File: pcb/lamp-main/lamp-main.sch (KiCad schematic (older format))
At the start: 29 parts, among them IC1 ATMEGA328P, IC2 DNP(LM1117_3.3), P1 VLED_IN, P10 V_IN, P2 AVR_ISP, P3 SERIAL, P4 LEDSTACK, P5 LEDSTACK, P6 LEDSTACK, P7 USER-INPUT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

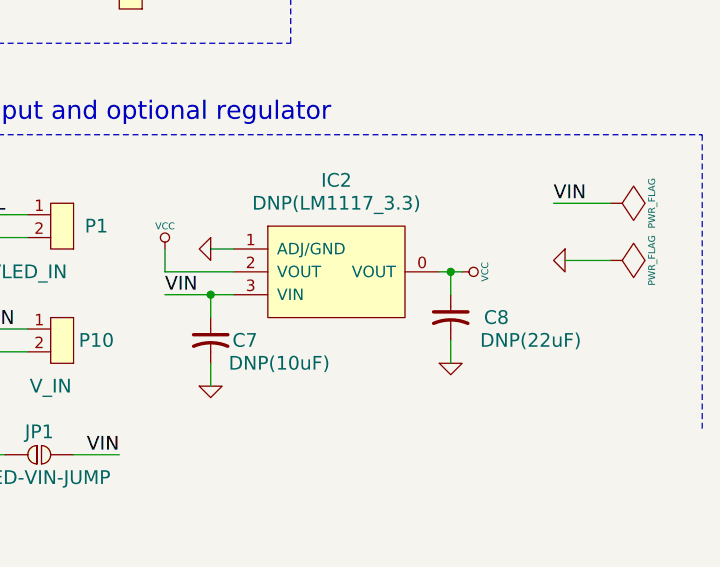
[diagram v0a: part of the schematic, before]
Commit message: add changes found after first iMac powerup since 2014
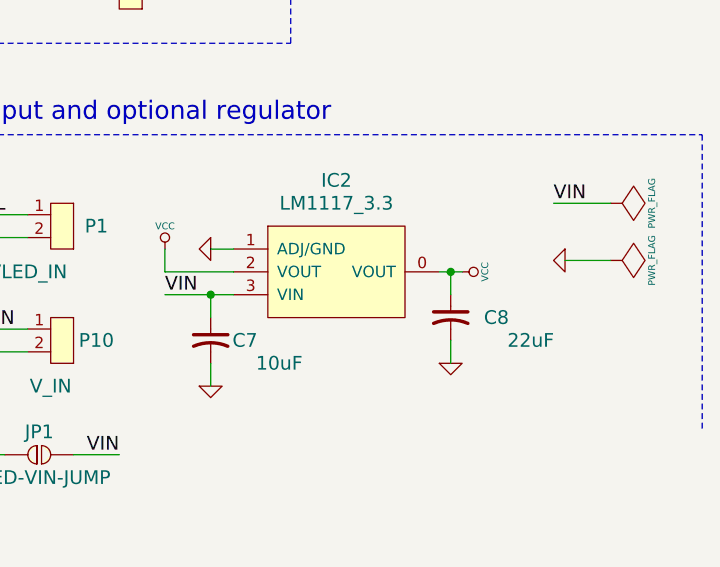
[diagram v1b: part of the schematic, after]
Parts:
- C1, C2, C3, C4, C5, C6, C9: footprint (none) -> capacitor:0603(1608m)-CHIP-CAP
- C7: value DNP(10uF) -> 10uF; footprint (none) -> capacitor:1206(3216m)-CHIP-CAP
- C8: value DNP(22uF) -> 22uF; footprint (none) -> capacitor:1206(3216m)-CHIP-CAP
- IC1: footprint (none) -> qfp:TQFP32_P0.8mm; Distrib. Link (none) -> http://www.digikey.com/product-detail/en/ATMEGA328P-AU/ATME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; Distrib. Part (none) -> ATMEGA328P-AU-ND; Distributor Link http://www.digikey.com/product-detail/en/ATMEGA328P-AU/ATME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 -> (none); Distributor Part ATMEGA328P-AU-ND -> (none); Manuf. Part (none) -> ATMEGA328P-AU; Manufacturer Part ATMEGA328P-AU -> (none)
- IC2: value DNP(LM1117_3.3) -> LM1117_3.3; footprint (none) -> sot:SOT223
- JP1: footprint (none) -> jumper:SOLDER-JUMPER_1-WAY
- LED1, LED2: footprint (none) -> led:0603(1608m)-SM-LED
- P1, P10, P8: footprint (none) -> sip:SIP2
- P2: footprint (none) -> connect-thru:2x3-ARRAY_P100mil
- P3: footprint (none) -> sip:SIP6
- P4, P5, P6, P7: footprint (none) -> sip:SIP5
- R1, R2, R3, R6, R7: footprint (none) -> resistor:0603(1608m)-CHIP-RESISTOR
- Y1: footprint (none) -> crystal:ABRACON-ABM2_xtal
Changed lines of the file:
@@
 F 0 "IC1" H 2650 3400 60  0000 C CNN
 F 1 "ATMEGA328P" H 3700 1050 60  0000 C CNN
-F 2 "" H 3350 2250 60  0000 C CNN
-F 3 "" H 3350 2250 60  0000 C CNN
+F 2 "qfp:TQFP32_P0.8mm" H 3350 2250 60  0001 C CNN
+F 3 "" H 3350 2250 60  0001 C CNN
 F 4 "Atmel" H 3350 2250 60  0001 C CNN "Manufacturer"
-F 5 "ATMEGA328P-AU" H 3350 2250 60  0001 C CNN "Manufacturer Part"
+F 5 "ATMEGA328P-AU" H 3350 2250 60  0001 C CNN "Manuf. Part"
 F 6 "Digikey" H 3350 2250 60  0001 C CNN "Distributor"
-F 7 "ATMEGA328P-AU-ND" H 3350 2250 60  0001 C CNN "Distributor Part"
-F 8 "http://www.digikey.com/product-detail/en/ATMEGA328P-AU/ATMEGA328P-AU-ND/1832260" H 3350 2250 60  0001 C CNN "Distributor Link"
+F 7 "ATMEGA328P-AU-ND" H 3350 2250 60  0001 C CNN "Distrib. Part"
+F 8 "http://www.digikey.com/product-detail/en/ATMEGA328P-AU/ATMEGA328P-AU-ND/1832260" H 3350 2250 60  0001 C CNN "Distrib. Link"
 	1    3350 2250
 	1    0    0    -1
@@
 F 0 "P2" H 1700 5300 60  0000 C CNN
 F 1 "AVR_ISP" H 2100 5300 60  0000 C CNN
-F 2 "" H 1950 5100 60  0001 C CNN
+F 2 "connect-thru:2x3-ARRAY_P100mil" H 1950 5100 60  0001 C CNN
 F 3 "" H 1950 5100 60  0001 C CNN
 	1    1950 5100
@@
 F 0 "P3" H 4050 5550 60  0000 C CNN
 F 1 "SERIAL" H 4000 5450 60  0000 C CNN
-F 2 "" H 4100 5050 60  0001 C CNN
+F 2 "sip:SIP6" H 4100 5050 60  0001 C CNN
 F 3 "" H 4100 5050 60  0001 C CNN
 	1    4050 5050
@@
 F 0 "Y1" V 2200 2700 60  0000 C CNN
 F 1 "8MHz" V 2100 2700 60  0000 C CNN
-F 2 "" H 2150 2500 60  0001 C CNN
+F 2 "crystal:ABRACON-ABM2_xtal" H 2150 2500 60  0001 C CNN
 F 3 "http://www.abracon.com/Resonators/abm2.pdf" H 2150 2500 60  0001 C CNN
 F 4 "Abracon Corporation" H 2150 2500 60  0001 C CNN "Manufacturer"
@@
 F 0 "C2" H 1350 2550 60  0000 C CNN
 F 1 "24pF" H 1600 2550 60  0000 C CNN
-F 2 "" H 1500 2400 60  0001 C CNN
+F 2 "capacitor:0603(1608m)-CHIP-CAP" H 1500 2400 60  0001 C CNN
 F 3 "" H 1500 2400 60  0001 C CNN
 F 4 "Samsung" H 1500 2400 60  0001 C CNN "Manufacturer"
@@
 F 0 "C6" H 1950 2450 60  0000 C CNN
 F 1 "0.1uF" H 1950 2350 60  0000 C CNN
-F 2 "" H 2100 2250 60  0001 C CNN
+F 2 "capacitor:0603(1608m)-CHIP-CAP" H 2100 2250 60  0001 C CNN
 F 3 "" H 2100 2250 60  0001 C CNN
 F 4 "On hand" H 2100 2250 60  0001 C CNN "Distributor"
@@
 F 0 "C1" V 1650 1750 60  0000 C CNN
 F 1 "0.1uF" V 1550 1750 60  0000 C CNN
-F 2 "" H 1350 1750 60  0001 C CNN
+F 2 "capacitor:0603(1608m)-CHIP-CAP" H 1350 1750 60  0001 C CNN
 F 3 "" H 1350 1750 60  0001 C CNN
 F 4 "On Hand" H 1350 1750 60  0001 C CNN "Distributor"
@@
 F 0 "C4" V 1950 1750 60  0000 C CNN
 F 1 "0.1uF" V 1850 1750 60  0000 C CNN
-F 2 "" H 1650 1750 60  0001 C CNN
+F 2 "capacitor:0603(1608m)-CHIP-CAP" H 1650 1750 60  0001 C CNN
 F 3 "" H 1650 1750 60  0001 C CNN
 F 4 "On hand" H 1650 1750 60  0001 C CNN "Distributor"
@@
 F 0 "C5" V 2250 1750 60  0000 C CNN
 F 1 "0.1uF" V 2150 1750 60  0000 C CNN
-F 2 "" H 1950 1750 60  0001 C CNN
+F 2 "capacitor:0603(1608m)-CHIP-CAP" H 1950 1750 60  0001 C CNN
 F 3 "" H 1950 1750 60  0001 C CNN
 F 4 "On hand" H 1950 1750 60  0001 C CNN "Distributor"
@@
 F 0 "P1" H 7350 3900 60  0000 C CNN
 F 1 "VLED_IN" H 7050 3700 60  0000 C CNN
-F 2 "" H 7100 3700 60  0001 C CNN
+F 2 "sip:SIP2" H 7100 3700 60  0001 C CNN
 F 3 "" H 7100 3700 60  0001 C CNN
 	1    7150 3900
@@
 P 8400 4100
 F 0 "IC2" H 8400 4500 60  0000 C CNN
-F 1 "DNP(LM1117_3.3)" H 8400 4400 60  0000 C CNN
-F 2 "" H 8400 4100 60  0001 C CNN
+F 1 "LM1117_3.3" H 8400 4400 60  0000 C CNN
+F 2 "sot:SOT223" H 8400 4100 60  0001 C CNN
 F 3 "http://www.diodes.com/datasheets/AZ1117C.pdf" H 8400 4100 60  0001 C CNN
 F 4 "Diodes Incorporated" H 8400 4100 60  0001 C CNN "Manufacturer"
@@
 P 7850 4400
 F 0 "C7" V 7850 4550 60  0000 C CNN
-F 1 "DNP(10uF)" V 7950 4700 60  0000 C CNN
-F 2 "" H 7850 4400 60  0001 C CNN
+F 1 "10uF" V 7950 4700 60  0000 C CNN
+F 2 "capacitor:1206(3216m)-CHIP-CAP" H 7850 4400 60  0001 C CNN
 F 3 "" H 7850 4400 60  0001 C CNN
 F 4 "Taiyo Yuden" H 7850 4400 60  0001 C CNN "Manufacturer"
@@
 P 8900 4300
 F 0 "C8" V 8900 4500 60  0000 C CNN
-F 1 "DNP(22uF)" V 9000 4650 60  0000 C CNN
-F 2 "" H 8900 4300 60  0001 C CNN
+F 1 "22uF" V 9000 4650 60  0000 C CNN
+F 2 "capacitor:1206(3216m)-CHIP-CAP" H 8900 4300 60  0001 C CNN
 F 3 "" H 8900 4300 60  0001 C CNN
 F 4 "Taiyo Yuden" H 8900 4300 60  0001 C CNN "Manufacturer"
@@
 F 0 "R2" H 5400 1400 60  0000 C CNN
 F 1 "10kΩ" H 5700 1400 60  0000 C CNN
-F 2 "" H 5350 1700 60  0001 C CNN
+F 2 "resistor:0603(1608m)-CHIP-RESISTOR" H 5350 1700 60  0001 C CNN
 F 3 "" H 5350 1700 60  0001 C CNN
 F 4 "On hand" H 5350 1700 60  0001 C CNN "Distributor"
@@
 F 0 "R3" H 5400 1500 60  0000 C CNN
 F 1 "10kΩ" H 5700 1500 60  0000 C CNN
-F 2 "" H 5350 1800 60  0001 C CNN
+F 2 "resistor:0603(1608m)-CHIP-RESISTOR" H 5350 1800 60  0001 C CNN
 F 3 "" H 5350 1800 60  0001 C CNN
 F 4 "On hand" H 5350 1800 60  0001 C CNN "Distributor"
@@
 F 0 "P4" H 7650 1500 60  0000 C CNN
 F 1 "LEDSTACK" H 7800 1400 60  0000 C CNN
-F 2 "" H 7500 1200 60  0001 C CNN
+F 2 "sip:SIP5" H 7500 1200 60  0001 C CNN
 F 3 "" H 7500 1200 60  0001 C CNN
 	1    7450 1300
@@
 F 0 "P5" H 7650 2200 60  0000 C CNN
 F 1 "LEDSTACK" H 7800 2100 60  0000 C CNN
-F 2 "" H 7500 1900 60  0001 C CNN
+F 2 "sip:SIP5" H 7500 1900 60  0001 C CNN
 F 3 "" H 7500 1900 60  0001 C CNN
 	1    7450 2000
@@
 F 0 "P6" H 7650 2900 60  0000 C CNN
 F 1 "LEDSTACK" H 7800 2800 60  0000 C CNN
-F 2 "" H 7500 2600 60  0001 C CNN
+F 2 "sip:SIP5" H 7500 2600 60  0001 C CNN
 F 3 "" H 7500 2600 60  0001 C CNN
 	1    7450 2700
@@
 F 0 "C3" H 1350 2450 60  0000 C CNN
 F 1 "24pF" H 1600 2450 60  0000 C CNN
-F 2 "" H 1500 2600 60  0001 C CNN
+F 2 "capacitor:0603(1608m)-CHIP-CAP" H 1500 2600 60  0001 C CNN
 F 3 "" H 1500 2600 60  0001 C CNN
 F 4 "Samsung Electro-Mechanics America, Inc" H 1500 2600 60  0001 C CNN "Manufacturer"
@@
 F 0 "R6" H 1950 3250 60  0000 C CNN
 F 1 "1kΩ" H 2150 3250 60  0000 C CNN
-F 2 "" H 2000 3350 60  0001 C CNN
+F 2 "resistor:0603(1608m)-CHIP-RESISTOR" H 2000 3350 60  0001 C CNN
 F 3 "" H 2000 3350 60  0001 C CNN
 F 4 "On hand" H 2000 3350 60  0001 C CNN "Distributor"
@@
 F 0 "LED1" H 1450 3450 60  0000 C CNN
 F 1 "RED" H 1750 3450 60  0000 C CNN
-F 2 "" H 1600 3350 60  0001 C CNN
+F 2 "led:0603(1608m)-SM-LED" H 1600 3350 60  0001 C CNN
 F 3 "" H 1600 3350 60  0001 C CNN
 F 4 "On hand" H 1600 3350 60  0001 C CNN "Distributor"
@@
 F 0 "R7" H 1950 3500 60  0000 C CNN
 F 1 "1kΩ" H 2150 3500 60  0000 C CNN
-F 2 "" H 2000 3600 60  0001 C CNN
+F 2 "resistor:0603(1608m)-CHIP-RESISTOR" H 2000 3600 60  0001 C CNN
 F 3 "" H 2000 3600 60  0001 C CNN
 F 4 "On hand" H 2000 3600 60  0001 C CNN "Distributor"
@@
 F 0 "LED2" H 1450 3700 60  0000 C CNN
 F 1 "RED" H 1750 3700 60  0000 C CNN
-F 2 "" H 1600 3600 60  0001 C CNN
+F 2 "led:0603(1608m)-SM-LED" H 1600 3600 60  0001 C CNN
 F 3 "" H 1600 3600 60  0001 C CNN
 F 4 "On hand" H 1600 3600 60  0001 C CNN "Distributor"
@@
 F 0 "R1" H 5400 1300 60  0000 C CNN
 F 1 "10kΩ" H 5700 1300 60  0000 C CNN
-F 2 "" H 5350 1600 60  0001 C CNN
+F 2 "resistor:0603(1608m)-CHIP-RESISTOR" H 5350 1600 60  0001 C CNN
 F 3 "" H 5350 1600 60  0001 C CNN
 F 4 "On hand" H 5350 1600 60  0001 C CNN "Distributor"
@@
 F 0 "C9" H 3450 5150 60  0000 C CNN
 F 1 "0.1uF" H 3700 5150 60  0000 C CNN
-F 2 "" H 3750 5300 60  0001 C CNN
+F 2 "capacitor:0603(1608m)-CHIP-CAP" H 3750 5300 60  0001 C CNN
 F 3 "" H 3750 5300 60  0001 C CNN
 F 4 "On hand" H 3750 5300 60  0001 C CNN "Distributor"
@@
 F 0 "P7" H 2300 6300 60  0000 C CNN
 F 1 "USER-INPUT" H 2100 6200 60  0000 C CNN
-F 2 "" H 2300 6550 60  0001 C CNN
+F 2 "sip:SIP5" H 2300 6550 60  0001 C CNN
 F 3 "" H 2300 6550 60  0001 C CNN
 	1    2250 6650
@@
 F 0 "P8" H 3500 6450 60  0000 C CNN
 F 1 "EXTRA-ADC" H 3350 6350 60  0000 C CNN
-F 2 "" H 3400 6450 60  0001 C CNN
+F 2 "sip:SIP2" H 3400 6450 60  0001 C CNN
 F 3 "" H 3400 6450 60  0001 C CNN
 	1    3450 6650
@@
 F 0 "P10" H 7350 4400 60  0000 C CNN
 F 1 "V_IN" H 7150 4200 60  0000 C CNN
-F 2 "" H 7100 4200 60  0001 C CNN
+F 2 "sip:SIP2" H 7100 4200 60  0001 C CNN
 F 3 "" H 7100 4200 60  0001 C CNN
 	1    7150 4400
@@
 F 0 "JP1" H 7100 5000 60  0000 C CNN
 F 1 "VLED-VIN-JUMP" H 7100 4800 60  0000 C CNN
-F 2 "" H 7000 4900 60  0001 C CNN
+F 2 "jumper:SOLDER-JUMPER_1-WAY" H 7000 4900 60  0001 C CNN
 F 3 "" H 7100 5000 60  0001 C CNN
 	1    7100 4900
